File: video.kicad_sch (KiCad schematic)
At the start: 56 parts, among them IC10 2318, IC11 MC14053, IC14 74LS86AN, IC21 74LS123N, IC22 74LS00N, IC23 74ALS74N, IC27 74LS20N, IC28 74LS393N, IC29 74LS393N, IC30 74LS32N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

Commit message: verify video logic
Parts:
- C7: footprint Capacitor_THT:C_Disc_D3.0mm_W2.0mm_P2.50mm -> Potentiometer_THT:Potentiometer_ACP_CA6-H2,5_Horizontal
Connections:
- net LUM CONTROL: now also IC22.9, IC23.8 (~{Q})
- net PULSE renamed LINE PULSES
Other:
- moved on the sheet: C25, C34, C6, IC10, IC11, IC14A, IC14B, IC14C, IC14D, IC21A, IC22C, IC22D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

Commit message: fix line pulse counter ic32
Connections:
- net at IC32.3 (Q0): no longer IC32.15 (~{CP0})
- net at IC32.9 (Q3): now also IC32.15 (~{CP0})

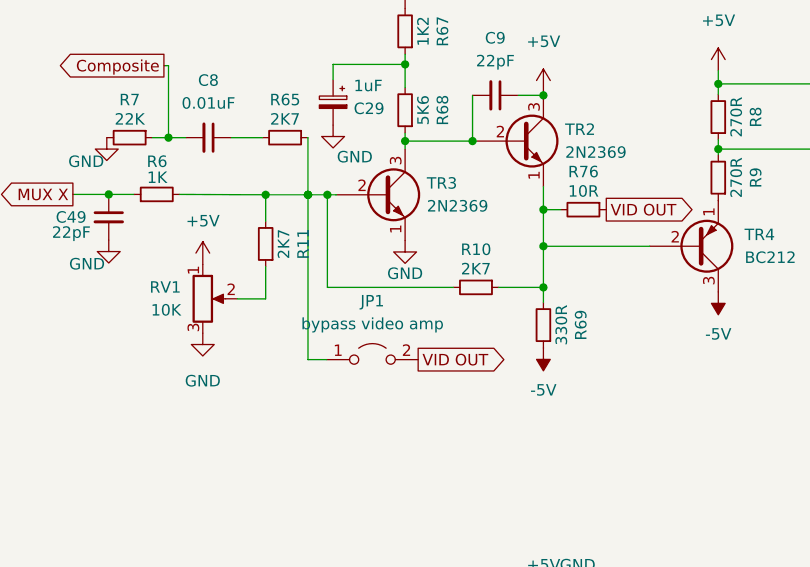
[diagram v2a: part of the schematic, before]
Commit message: reroute video circuit
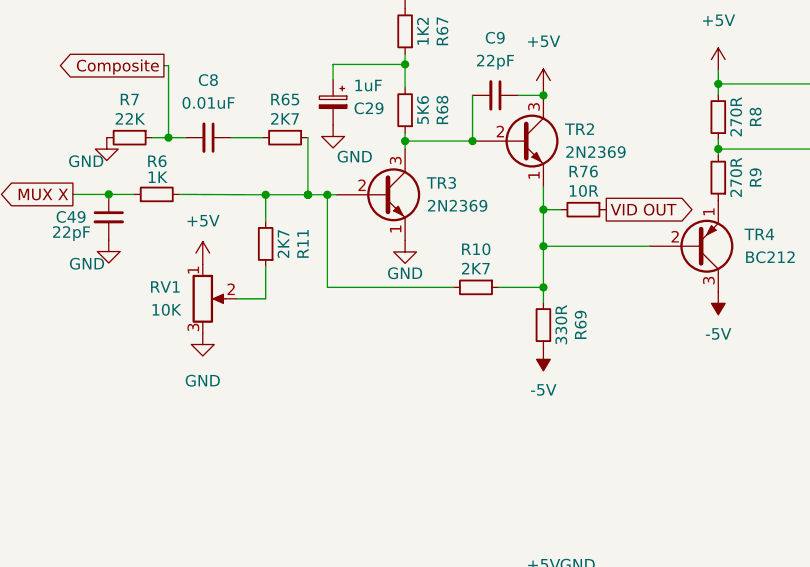
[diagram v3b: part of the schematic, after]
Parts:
- removed JP1: bypass video amp, Jumper:SolderJumper-2_P1.3mm_Open_TrianglePad1.0x1.5mm, symbol Jumper:Jumper_2_Open

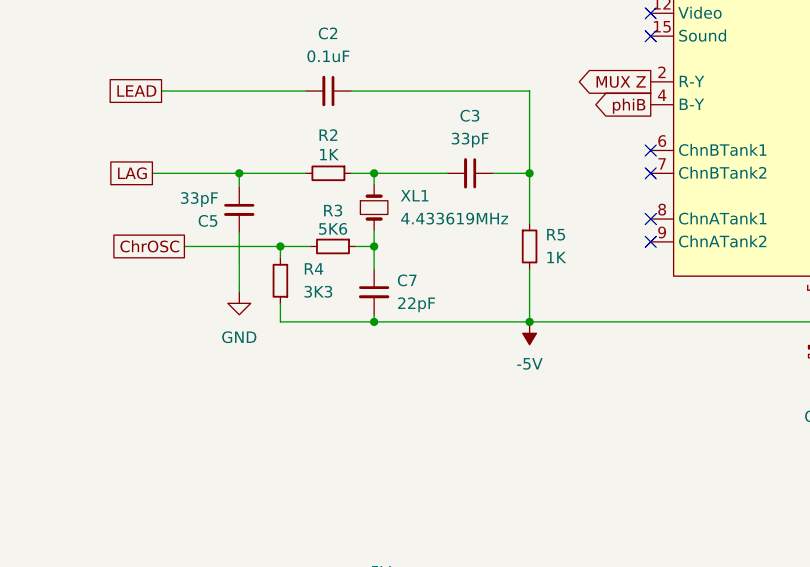
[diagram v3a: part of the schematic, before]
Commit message: reroute power
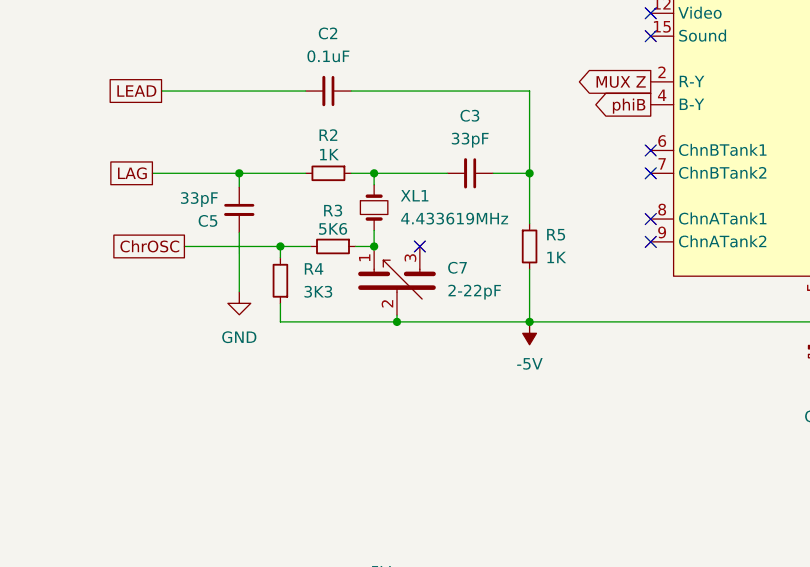
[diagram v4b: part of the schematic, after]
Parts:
- removed C7: 22pF, Potentiometer_THT:Potentiometer_ACP_CA6-H2,5_Horizontal, symbol Device:C_Small
- added C7: 2-22pF, Potentiometer_THT:Potentiometer_ACP_CA6-H2,5_Horizontal, symbol Device:C_Trim_Differential
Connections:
- net -5V: now also C7.2
- net at R3.1, XL1.2: now also C7.1
- no-connect marks 35 -> 36
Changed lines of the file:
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@@
   (paper "A3")
   (title_block
-    (date "2022-10-19")
-    (rev "1.5")
+    (date "2022-12-29")
+    (rev "1.6")
     (comment 2 "Reposition dram and buffer")
   )
@@
   (junction (at 337.312 44.45) (diameter 0) (color 0 0 0 0)
   )
+  (junction (at 306.451 42.799) (diameter 0) (color 0 0 0 0)
+  )
+  (junction (at 204.343 258.445) (diameter 0) (color 0 0 0 0)
+  )
+  (junction (at 313.309 42.799) (diameter 0) (color 0 0 0 0)
+  )
+  (junction (at 176.276 118.364) (diameter 0) (color 0 0 0 0)
+  )
+  (junction (at 295.656 36.449) (diameter 0) (color 0 0 0 0)
+  )
+  (junction (at 70.485 259.969) (diameter 0) (color 0 0 0 0)
+  )
+  (junction (at 30.988 167.4252) (diameter 0) (color 0 0 0 0)
+  )
+  (junction (at 151.511 170.688) (diameter 0) (color 0 0 0 0)
+  )
+  (junction (at 124.714 257.429) (diameter 0) (color 0 0 0 0)
+  )
+  (junction (at 211.328 62.23) (diameter 0) (color 0 0 0 0)
+  )
+  (junction (at 321.945 36.83) (diameter 0) (color 0 0 0 0)
+  )
+  (junction (at 125.73 254.889) (diameter 0) (color 0 0 0 0)
+  )
+  (junction (at 148.59 109.982) (diameter 0) (color 0 0 0 0)
+  )
+  (junction (at 47.244 234.9679) (diameter 0) (color 0 0 0 0)
+  )
+  (junction (at 149.987 266.192) (diameter 0) (color 0 0 0 0)
+  )
+  (junction (at 176.276 101.854) (diameter 0) (color 0 0 0 0)
+  )
+  (junction (at 159.004 101.854) (diameter 0) (color 0 0 0 0)
+  )
+  (junction (at 356.743 30.48) (diameter 0) (color 0 0 0 0)
+  )
+  (junction (at 38.862 167.4252) (diameter 0) (color 0 0 0 0)
+  )
+  (junction (at 168.783 238.633) (diameter 0) (color 0 0 0 0)
+  )
+  (junction (at 65.913 167.386) (diameter 0) (color 0 0 0 0)
+  )
+  (junction (at 337.312 48.514) (diameter 0) (color 0 0 0 0)
+  )
+  (junction (at 311.15 42.799) (diameter 0) (color 0 0 0 0)
+  )
+  (junction (at 42.418 230.886) (diameter 0) (color 0 0 0 0)
+  )
+  (junction (at 287.655 112.776) (diameter 0) (color 0 0 0 0)
+  )
+  (junction (at 287.655 101.727) (diameter 0) (color 0 0 0 0)
+  )
+  (junction (at 168.783 221.361) (diameter 0) (color 0 0 0 0)
+  )
+  (junction (at 321.945 28.3122) (diameter 0) (color 0 0 0 0)
+  )
+  (junction (at 337.312 31.75) (diameter 0) (color 0 0 0 0)
+  )
+  (junction (at 305.689 101.727) (diameter 0) (color 0 0 0 0)
+  )
+  (junction (at 159.004 157.988) (diameter 0) (color 0 0 0 0)
+  )
+  (junction (at 149.987 250.063) (diameter 0) (color 0 0 0 0)
+  )
+  (junction (at 35.5139 159.766) (diameter 0) (color 0 0 0 0)
+  )
+  (junction (at 76.708 189.865) (diameter 0) (color 0 0 0 0)
+  )
+  (junction (at 311.1548 42.799) (diameter 0) (color 0 0 0 0)
+  )
+  (junction (at 273.05 112.776) (diameter 0) (color 0 0 0 0)
+  )
+  (junction (at 161.544 118.364) (diameter 0) (color 0 0 0 0)
+  )
+  (junction (at 356.743 37.719) (diameter 0) (color 0 0 0 0)
+  )
   (junction (at 159.004 109.982) (diameter 0) (color 0 0 0 0)
-  )
-  (junction (at 306.451 42.799) (diameter 0) (color 0 0 0 0)
-  )
-  (junction (at 204.343 258.445) (diameter 0) (color 0 0 0 0)
-  )
-  (junction (at 313.309 42.799) (diameter 0) (color 0 0 0 0)
-  )
-  (junction (at 176.276 118.364) (diameter 0) (color 0 0 0 0)
-  )
-  (junction (at 295.656 36.449) (diameter 0) (color 0 0 0 0)
-  )
-  (junction (at 70.485 259.969) (diameter 0) (color 0 0 0 0)
-  )
-  (junction (at 30.988 167.4252) (diameter 0) (color 0 0 0 0)
-  )
-  (junction (at 151.511 170.688) (diameter 0) (color 0 0 0 0)
-  )
-  (junction (at 124.714 257.429) (diameter 0) (color 0 0 0 0)
-  )
-  (junction (at 211.328 62.23) (diameter 0) (color 0 0 0 0)
-  )
-  (junction (at 321.945 36.83) (diameter 0) (color 0 0 0 0)
-  )
-  (junction (at 125.73 254.889) (diameter 0) (color 0 0 0 0)
-  )
-  (junction (at 148.59 109.982) (diameter 0) (color 0 0 0 0)
-  )
-  (junction (at 47.244 234.9679) (diameter 0) (color 0 0 0 0)
-  )
-  (junction (at 149.987 266.192) (diameter 0) (color 0 0 0 0)
-  )
-  (junction (at 176.276 101.854) (diameter 0) (color 0 0 0 0)
-  )
-  (junction (at 159.004 101.854) (diameter 0) (color 0 0 0 0)
-  )
-  (junction (at 356.743 30.48) (diameter 0) (color 0 0 0 0)
-  )
-  (junction (at 38.862 167.4252) (diameter 0) (color 0 0 0 0)
-  )
-  (junction (at 168.783 238.633) (diameter 0) (color 0 0 0 0)
-  )
-  (junction (at 65.913 167.386) (diameter 0) (color 0 0 0 0)
-  )
-  (junction (at 337.312 48.514) (diameter 0) (color 0 0 0 0)
-  )
-  (junction (at 311.15 42.799) (diameter 0) (color 0 0 0 0)
-  )
-  (junction (at 42.418 230.886) (diameter 0) (color 0 0 0 0)
-  )
-  (junction (at 287.655 112.776) (diameter 0) (color 0 0 0 0)
-  )
-  (junction (at 287.655 101.727) (diameter 0) (color 0 0 0 0)
-  )
-  (junction (at 168.783 221.361) (diameter 0) (color 0 0 0 0)
-  )
-  (junction (at 321.945 28.3122) (diameter 0) (color 0 0 0 0)
-  )
-  (junction (at 337.312 31.75) (diameter 0) (color 0 0 0 0)
-  )
-  (junction (at 305.689 101.727) (diameter 0) (color 0 0 0 0)
-  )
-  (junction (at 159.004 157.988) (diameter 0) (color 0 0 0 0)
-  )
-  (junction (at 149.987 250.063) (diameter 0) (color 0 0 0 0)
-  )
-  (junction (at 35.5139 159.766) (diameter 0) (color 0 0 0 0)
-  )
-  (junction (at 76.708 189.865) (diameter 0) (color 0 0 0 0)
-  )
-  (junction (at 311.1548 42.799) (diameter 0) (color 0 0 0 0)
-  )
-  (junction (at 273.05 112.776) (diameter 0) (color 0 0 0 0)
-  )
-  (junction (at 159.004 118.364) (diameter 0) (color 0 0 0 0)
-  )
-  (junction (at 356.743 37.719) (diameter 0) (color 0 0 0 0)
   )
   (junction (at 30.988 167.386) (diameter 0) (color 0 0 0 0)
@@
   (no_connect (at 95.885 247.269))
   (no_connect (at 139.065 223.901))
+  (no_connect (at 164.084 109.982))
   (no_connect (at 227.838 77.724))
   (no_connect (at 348.488 208.026))
@@
     (stroke (width 0) (type default) (color 0 0 0 0))
   )
-  (wire (pts (xy 159.004 117.602) (xy 159.004 118.364))
-    (stroke (width 0) (type default) (color 0 0 0 0))
-  )
   (wire (pts (xy 305.689 115.316) (xy 305.689 101.727))
     (stroke (width 0) (type default) (color 0 0 0 0))
@@
     (stroke (width 0) (type default) (color 0 0 0 0))
   )
-  (wire (pts (xy 159.004 118.364) (xy 176.276 118.364))
+  (wire (pts (xy 148.59 118.364) (xy 161.544 118.364))
     (stroke (width 0) (type default) (color 0 0 0 0))
   )
@@
     (stroke (width 0) (type default) (color 0 0 0 0))
   )
+  (wire (pts (xy 161.544 117.602) (xy 161.544 118.364))
+    (stroke (width 0) (type default) (color 0 0 0 0))
+  )
   (wire (pts (xy 295.148 28.448) (xy 295.656 28.448))
     (stroke (width 0) (type default) (color 0 0 0 0))
@@
     (stroke (width 0) (type default) (color 0 0 0 0))
   )
-  (wire (pts (xy 159.004 109.982) (xy 159.004 112.522))
-    (stroke (width 0) (type default) (color 0 0 0 0))
-  )
   (wire (pts (xy 171.323 255.905) (xy 171.323 258.445))
     (stroke (width 0) (type default) (color 0 0 0 0))
@@
     (stroke (width 0) (type default) (color 0 0 0 0))
   )
-  (wire (pts (xy 148.59 118.364) (xy 159.004 118.364))
-    (stroke (width 0) (type default) (color 0 0 0 0))
-  )
   (wire (pts (xy 123.698 266.7) (xy 36.576 266.7))
     (stroke (width 0) (type default) (color 0 0 0 0))
@@
   )
   (wire (pts (xy 176.276 112.522) (xy 176.276 118.364))
+    (stroke (width 0) (type default) (color 0 0 0 0))
+  )
+  (wire (pts (xy 161.544 118.364) (xy 176.276 118.364))
     (stroke (width 0) (type default) (color 0 0 0 0))
   )
@@
     (pin "2")
   )
-  (symbol (lib_id "Device:C_Small") (at 159.004 115.062 0) (unit 1)
-    (in_bom yes) (on_board yes) (fields_autoplaced)
-    (property "Reference" "C7" (id 0) (at 161.544 113.7982 0)
-      (effects (font (size 1.27 1.27)) (justify left))
-    )
-    (property "Value" "22pF" (id 1) (at 161.544 116.3382 0)
-      (effects (font (size 1.27 1.27)) (justify left))
-    )
-    (property "Footprint" "Potentiometer_THT:Potentiometer_ACP_CA6-H2,5_Horizontal" (id 2) (at 159.004 115.062 0)
-      (effects (font (size 1.27 1.27)) hide)
-    )
-    (property "Datasheet" "https://connect.kemet.com:7667/gateway/IntelliData-ComponentDocumentation/1.0/download/datasheet/C315C220K2G5TA7301" (id 3) (at 159.004 115.062 0)
-      (effects (font (size 1.27 1.27)) hide)
-    )
-    (property "Note" "Spec is 2-22pF" (id 4) (at 159.004 115.062 0)
-      (effects (font (size 1.27 1.27)) hide)
-    )
-    (property "DigiKey" "399-13930-1-ND" (id 5) (at 159.004 115.062 0)
-      (effects (font (size 1.27 1.27)) hide)
-    )
-    (pin "1")
-    (pin "2")
-  )
   (symbol (lib_id "power:GND") (at 204.343 263.525 0) (unit 1)
     (in_bom yes) (on_board yes) (fields_autoplaced)
@@
     (pin "1")
   )
+  (symbol (lib_id "Device:C_Trim_Differential") (at 161.544 113.792 0) (unit 1)
+    (in_bom yes) (on_board yes) (fields_autoplaced)
+    (property "Reference" "C7" (id 0) (at 167.132 112.3949 0)
+      (effects (font (size 1.27 1.27)) (justify left))
+    )
+    (property "Value" "2-22pF" (id 1) (at 167.132 114.9349 0)
+      (effects (font (size 1.27 1.27)) (justify left))
+    )
+    (property "Footprint" "Potentiometer_THT:Potentiometer_ACP_CA6-H2,5_Horizontal" (id 2) (at 161.544 113.792 0)
+      (effects (font (size 1.27 1.27)) hide)
+    )
+    (property "Datasheet" "https://connect.kemet.com:7667/gateway/IntelliData-ComponentDocumentation/1.0/download/datasheet/C315C220K2G5TA7301" (id 3) (at 161.544 113.792 0)
+      (effects (font (size 1.27 1.27)) hide)
+    )
+    (pin "1")
+    (pin "2")
+    (pin "3")
+  )
   (symbol (lib_id "74xx:74LS390") (at 116.713 221.361 180) (unit 2)
